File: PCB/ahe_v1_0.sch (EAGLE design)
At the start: 16 parts, among them CN1 1X4-BIG, CN3 1X4SMT, IC1 MS560702BA03-50, IC2 MCP73871-1CCI_ML, J1 USB3075-30-A

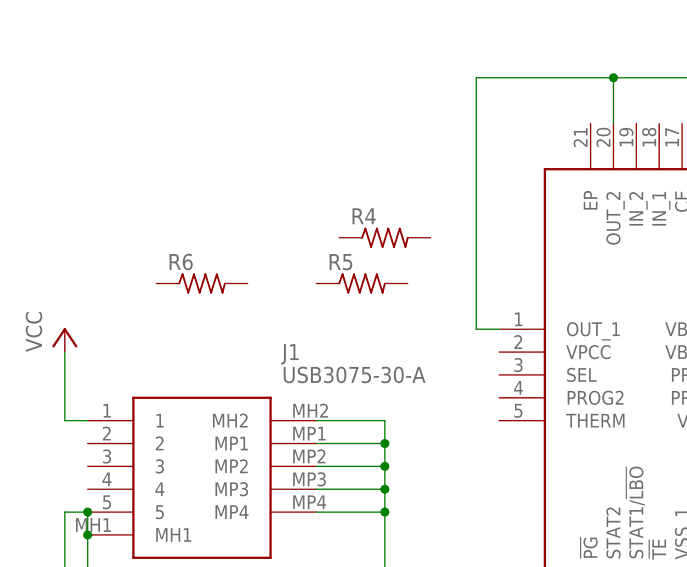
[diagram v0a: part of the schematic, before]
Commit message: updated the readme with eagle usage instructions
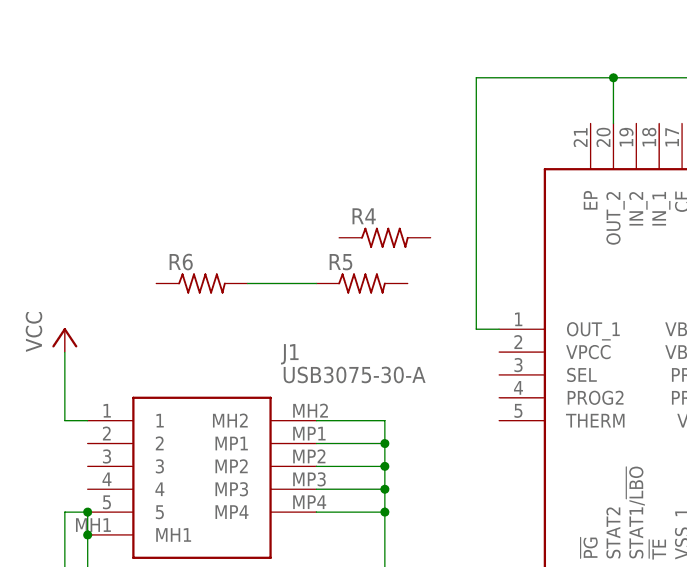
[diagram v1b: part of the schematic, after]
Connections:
- new net N$3: R5.1, R6.2
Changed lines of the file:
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@@
+</segment>
+</net>
+<net name="N$3" class="0">
+<segment>
+<pinref part="R6" gate="G$1" pin="2"/>
+<pinref part="R5" gate="G$1" pin="1"/>
+<wire x1="-73.66" y1="139.7" x2="-66.04" y2="139.7" width="0.1524" layer="91"/>
 </segment>
 </net>

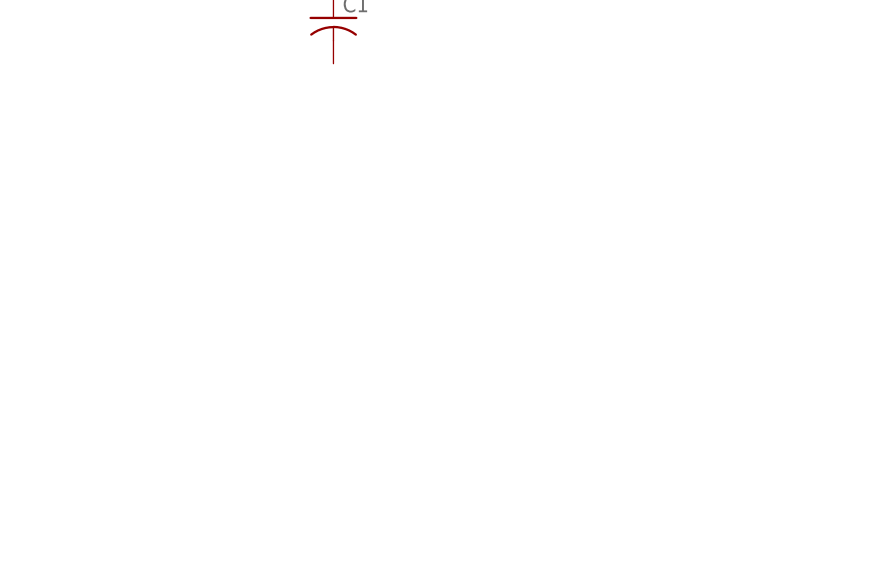
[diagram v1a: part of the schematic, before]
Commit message: added an LDO
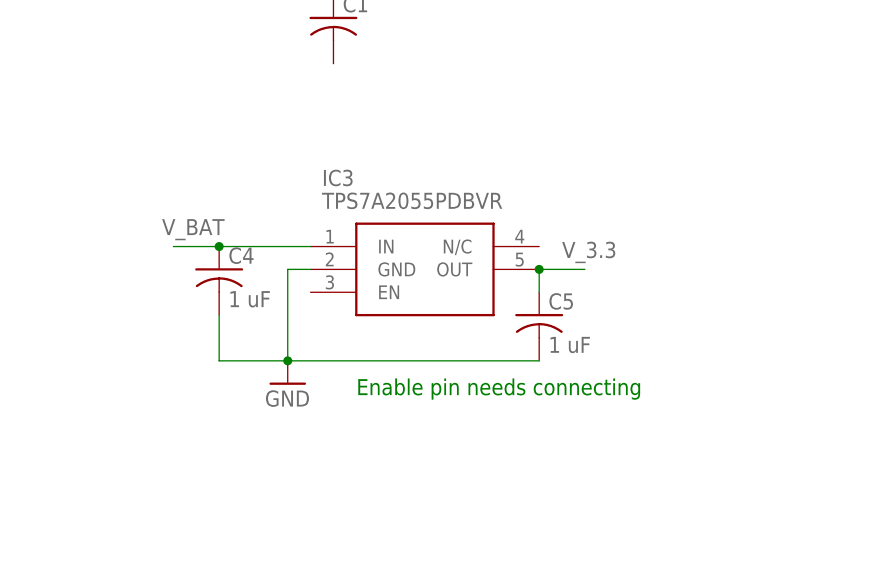
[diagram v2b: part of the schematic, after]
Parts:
- added C4, C5: 1 uF, rcl:C-USC0805
- added IC3: TPS7A2055PDBVR, TPS7A2055PDBVR:TPS7A2055PDBVR
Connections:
- new net V_3.3: C5.1, IC3.OUT
- new net V_BAT: C4.1, IC3.IN
- net GND: now also C4.2, C5.2, IC3.GND
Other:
- note added: "Enable pin needs connecting"
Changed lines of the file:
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@@
 <setting verticaltext="up"/>
 </settings>
-<grid distance="0.1" unitdist="inch" unit="inch" style="lines" multiple="1" display="no" altdistance="0.01" altunitdist="inch" altunit="inch"/>
+<grid distance="0.05" unitdist="inch" unit="inch" style="lines" multiple="1" display="yes" altdistance="0.01" altunitdist="inch" altunit="inch"/>
 <layers>
 <layer number="1" name="Top" color="4" fill="1" visible="no" active="no"/>
@@
 <part name="GND2" library="supply1" library_urn="urn:adsk.eagle:library:371" deviceset="GND" device=""/>
 <part name="GND3" library="supply1" library_urn="urn:adsk.eagle:library:371" deviceset="GND" device=""/>
+<part name="IC3" library="TPS7A2055PDBVR" deviceset="TPS7A2055PDBVR" device=""/>
+<part name="C4" library="rcl" library_urn="urn:adsk.eagle:library:334" deviceset="C-US" device="C0805" package3d_urn="urn:adsk.eagle:package:23617/2" value="1 uF"/>
+<part name="C5" library="rcl" library_urn="urn:adsk.eagle:library:334" deviceset="C-US" device="C0805" package3d_urn="urn:adsk.eagle:package:23617/2" value="1 uF"/>
+<part name="GND4" library="supply1" library_urn="urn:adsk.eagle:library:371" deviceset="GND" device=""/>
 </parts>
 <sheets>
@@
 <plain>
 <text x="78.74" y="124.46" size="1.778" layer="91">Pressure - Sensor</text>
+<text x="-60.96" y="52.07" size="1.778" layer="91">Enable pin needs connecting </text>
 </plain>
 <instances>
@@
 <instance part="GND3" gate="1" x="20.32" y="116.84" smashed="yes">
 <attribute name="VALUE" x="17.78" y="114.3" size="1.778" layer="96"/>
+</instance>
+<instance part="IC3" gate="G$1" x="-66.04" y="68.58" smashed="yes">
+<attribute name="NAME" x="-64.77" y="76.2" size="1.778" layer="95" align="center-left"/>
+<attribute name="VALUE" x="-64.77" y="73.66" size="1.778" layer="96" align="center-left"/>
+</instance>
+<instance part="C4" gate="G$1" x="-76.2" y="66.04" smashed="yes">
+<attribute name="NAME" x="-75.184" y="66.675" size="1.778" layer="95"/>
+<attribute name="VALUE" x="-75.184" y="61.849" size="1.778" layer="96"/>
+</instance>
+<instance part="C5" gate="G$1" x="-40.64" y="60.96" smashed="yes">
+<attribute name="NAME" x="-39.624" y="61.595" size="1.778" layer="95"/>
+<attribute name="VALUE" x="-39.624" y="56.769" size="1.778" layer="96"/>
+</instance>
+<instance part="GND4" gate="1" x="-68.58" y="53.34" smashed="yes">
+<attribute name="VALUE" x="-71.12" y="50.8" size="1.778" layer="96"/>
 </instance>
 </instances>
@@
 <junction x="20.32" y="129.54"/>
 </segment>
+<segment>
+<pinref part="IC3" gate="G$1" pin="GND"/>
+<wire x1="-66.04" y1="66.04" x2="-68.58" y2="66.04" width="0.1524" layer="91"/>
+<pinref part="GND4" gate="1" pin="GND"/>
+<wire x1="-68.58" y1="66.04" x2="-68.58" y2="55.88" width="0.1524" layer="91"/>
+<pinref part="C4" gate="G$1" pin="2"/>
+<wire x1="-76.2" y1="60.96" x2="-76.2" y2="55.88" width="0.1524" layer="91"/>
+<wire x1="-76.2" y1="55.88" x2="-68.58" y2="55.88" width="0.1524" layer="91"/>
+<junction x="-68.58" y="55.88"/>
+<pinref part="C5" gate="G$1" pin="2"/>
+<wire x1="-40.64" y1="55.88" x2="-68.58" y2="55.88" width="0.1524" layer="91"/>
+</segment>
 </net>
 <net name="N$1" class="0">
@@
 </segment>
 </net>
+<net name="V_BAT" class="0">
+<segment>
+<pinref part="IC3" gate="G$1" pin="IN"/>
+<pinref part="C4" gate="G$1" pin="1"/>
+<wire x1="-66.04" y1="68.58" x2="-76.2" y2="68.58" width="0.1524" layer="91"/>
+<label x="-82.55" y="69.85" size="1.778" layer="95"/>
+<wire x1="-76.2" y1="68.58" x2="-81.28" y2="68.58" width="0.1524" layer="91"/>
+<junction x="-76.2" y="68.58"/>
+</segment>
+</net>
+<net name="V_3.3" class="0">
+<segment>
+<pinref part="IC3" gate="G$1" pin="OUT"/>
+<pinref part="C5" gate="G$1" pin="1"/>
+<wire x1="-40.64" y1="66.04" x2="-40.64" y2="63.5" width="0.1524" layer="91"/>
+<label x="-38.1" y="67.31" size="1.778" layer="95"/>
+<wire x1="-40.64" y1="66.04" x2="-35.56" y2="66.04" width="0.1524" layer="91"/>
+<junction x="-40.64" y="66.04"/>
+</segment>
+</net>

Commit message: added some cosmatics to completed parts
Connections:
- removed net V_BAT: C4.1, IC3.IN
- net GND: now also IC3.EN
- net VDD: now also C4.1, IC3.IN
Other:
- note added: "Power Regulation"
- note removed: "Enable pin needs connecting"
- moved on the sheet: C1, CN1, CN3, IC1, J1
